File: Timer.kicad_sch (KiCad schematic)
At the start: 17 parts

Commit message: WIP solving ERC issues
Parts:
- added 10k211, 10k212, 10k213, 10k214, 10k215: R, symbol z80-rescue:R
- P202: renamed from P?; symbol z80-rescue:CONN_01X04 -> Connector:Conn_01x04_Pin
- gave numbers to parts that had none: 7
- renumbered 10k to 10k201, 10k to 10k202, 10k to 10k203, 10k to 10k204, 10k to 10k205, 10k to 10k206, 10k to 10k207, 10k to 10k208, 10k to 10k210
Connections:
- net A0: now also U202.34 (B/~{A})
- net A1: now also U202.33 (C/~{D})
- net CLK: now also U202.20 (CLK)
- net GND: now also U201.5 (GND), U202.31 (GND), 10k211.1
- net VCC: now also U201.24 (VCC), U202.9 (VCC), 10k212.1, 10k213.1, 10k214.1, 10k215.1
- net ~{RESET}: now also U202.21 (~{RESET})
- net D4: now reaches U201.1 (D4)
- net D4: now also U202.38 (D4)
- net ~{IORQ}: now reaches U201.10 (~{IORQ})
- net ~{IORQ}: now also U202.36 (~{IORQ})
- net IEO_CTC: now reaches P202.3 (Pin_3), U201.11 (IEO)
- net ~{INT_CTC}: now reaches P202.2 (Pin_2), U201.12 (~{INT})
- net IEI_CTC: now reaches P202.4 (Pin_4), U201.13 (IEI)
- net ~{M1}: now reaches U201.14 (~{M1})
- net ~{M1}: now also U202.8 (~{M1})
- net D5: now reaches U201.2 (D5)
- net D5: now also U202.3 (D5)
- net D0: now reaches U201.25 (D0)
- net D0: now also U202.40 (D0)
- net D1: now reaches U201.26 (D1)
- net D1: now also U202.1 (D1)
- net D2: now reaches U201.27 (D2)
- net D2: now also U202.39 (D2)
- net D3: now reaches U201.28 (D3)
- net D3: now also U202.2 (D3)
- net D6: now reaches U201.3 (D6)
- net D6: now also U202.37 (D6)
- net D7: now reaches U201.4 (D7)
- net D7: now also U202.4 (D7)
- net ~{RD}: now reaches U201.6 (~{RD})
- net ~{RD}: now also U202.32 (~{RD})
- net ZC/TO0: now reaches P204.1 (P1), U201.7 (ZC/TO0)
- net ZC/TO1: now reaches P204.2 (P2), U201.8 (ZC/TO1)
- net ZC/TO2: now reaches P204.3 (P3), U201.9 (ZC/TO2)
- net TxDA: now reaches P203.11 (P11)
- net TxDA: now also U202.15 (TxDA); no longer U202.10 (~{W}/~{RDYA})
- net ~{SYNCA}: now reaches 10k203.2, U202.11 (~{SYNCA})
- net ~{SYNCA}: now also P203.3 (P3); no longer P203.9 (P9)
- net RxDA: now reaches 10k209.2, U202.12 (RxDA)
- net RxDA: now also P203.5 (P5); no longer P203.1 (P1)
- net ~{RxCA}: now reaches 10k201.2, U202.13 (~{RxCA})
- net ~{RxCA}: now also P203.7 (P7); no longer P203.3 (P3)
- net ~{TxCA}: now reaches 10k202.2, U202.14 (~{TxCA})
- net ~{TxCA}: now also P203.9 (P9); no longer P203.7 (P7)
- net ~{CTSA}: now reaches P203.17 (P17)
- net ~{CTSA}: now also 10k204.2, U202.18 (~{CTSA}); no longer U202.16 (~{DTRA})
- net ~{DTRA}: now reaches P203.13 (P13)
- net ~{DTRA}: now also U202.16 (~{DTRA}); no longer U202.17 (~{RTSA})
- net ~{DCDA}: now reaches 10k206.2, P203.19 (P19), U202.19 (~{DCDA})
- net ~{DCDB}: now reaches U202.22 (~{DCDB})
- net ~{DCDB}: now also P203.18 (P18), 10k215.2
- net ~{CTSB}: now reaches U202.23 (~{CTSB})
- net ~{CTSB}: now also P203.16 (P16), 10k214.2
- net ~{RTSB}: now reaches U202.24 (~{RTSB})
- net ~{RTSB}: now also P203.14 (P14)
- net ~{DTRB}: now reaches U202.25 (~{DTRB})
- net ~{DTRB}: now also P203.12 (P12)
- net TxDB: now reaches U202.26 (TxDB)
- net TxDB: now also P203.10 (P10)
- net ~{RxTxCB}: now reaches U202.27 (~{RxTxCB})
- net ~{RxTxCB}: now also P203.8 (P8), 10k212.2
- net RxDB: now reaches U202.28 (RxDB)
- net RxDB: now also P203.6 (P6), 10k211.2
- net ~{SYNCB}: now reaches U202.29 (~{SYNCB})
- net ~{SYNCB}: now also P203.4 (P4), 10k213.2
- net ~{W}/~{RDYB}: now reaches U202.30 (~{W}/~{RDYB})
- net ~{W}/~{RDYB}: now also P203.2 (P2)
- net ~{SIO_CE}: now reaches U202.35 (~{CE})
- net ~{CE1} renamed ~{CTC_CE}
- new net ~{RTSA}: P203.15 (P15), U202.17 (~{RTSA})
- new net ~{W}/~{RDYA}: P203.1 (P1), U202.10 (~{W}/~{RDYA})
- no-connect marks 0 -> 1
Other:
- moved on the sheet: 10k201, 10k202, 10k203, 10k204, 10k206, 10k209, P203

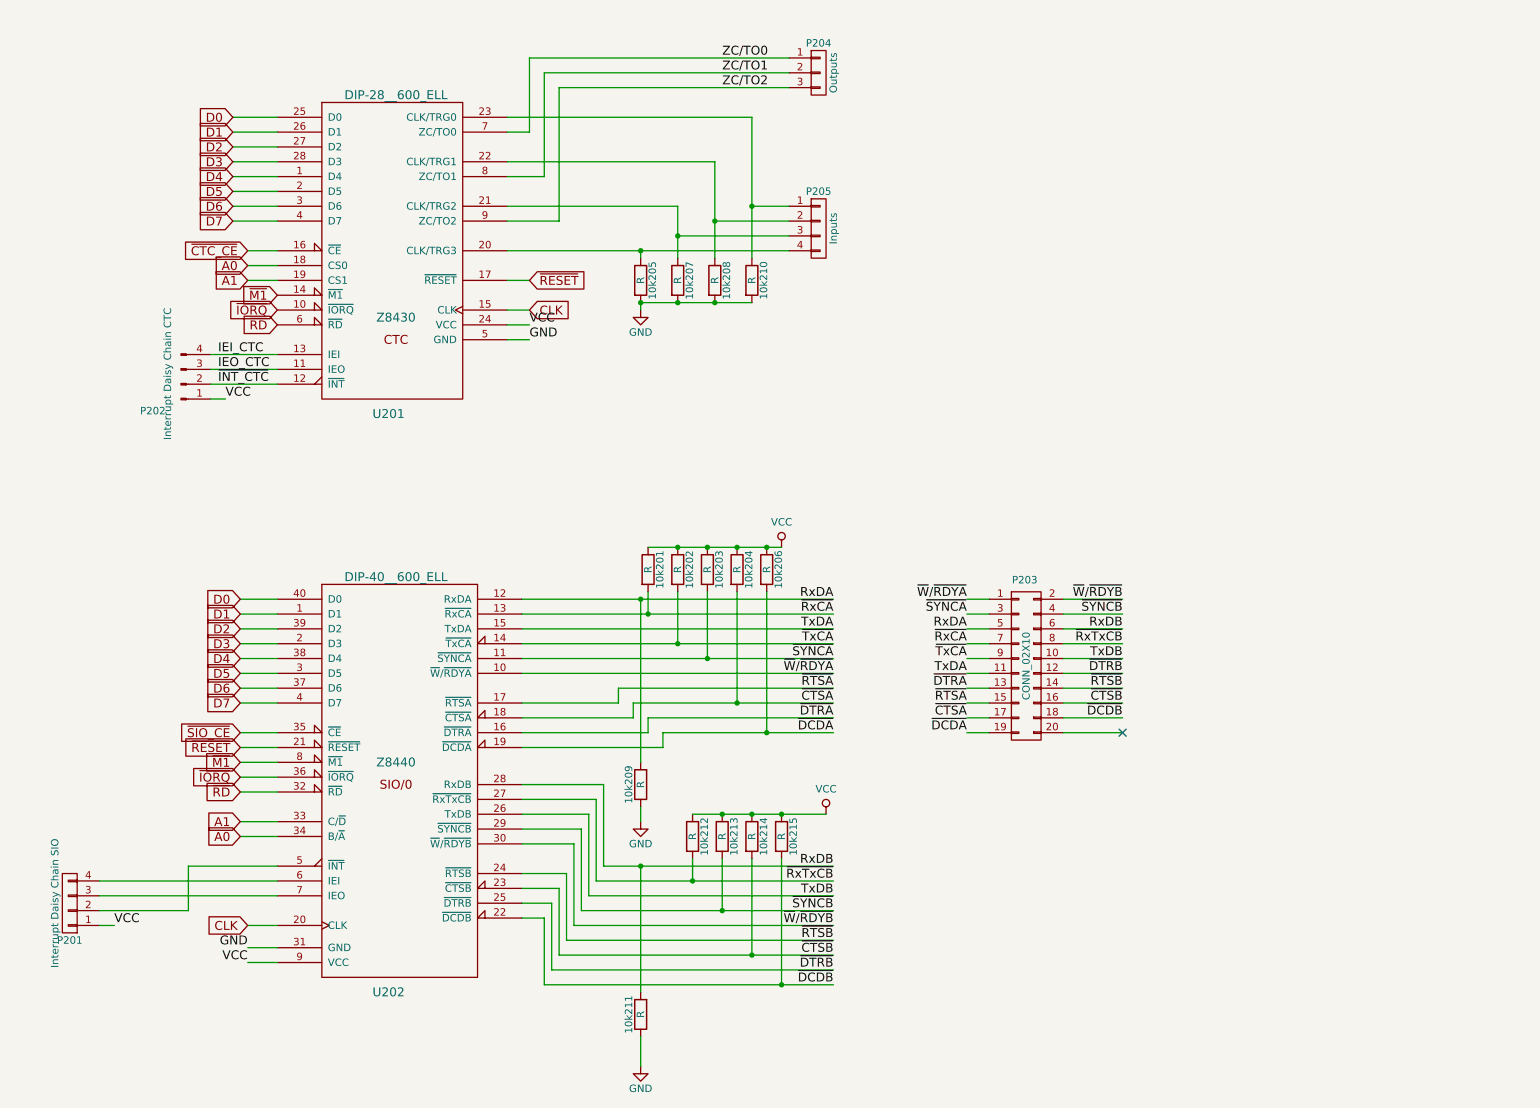
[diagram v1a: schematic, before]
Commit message: Fixed all schematic ERC errors and warnings
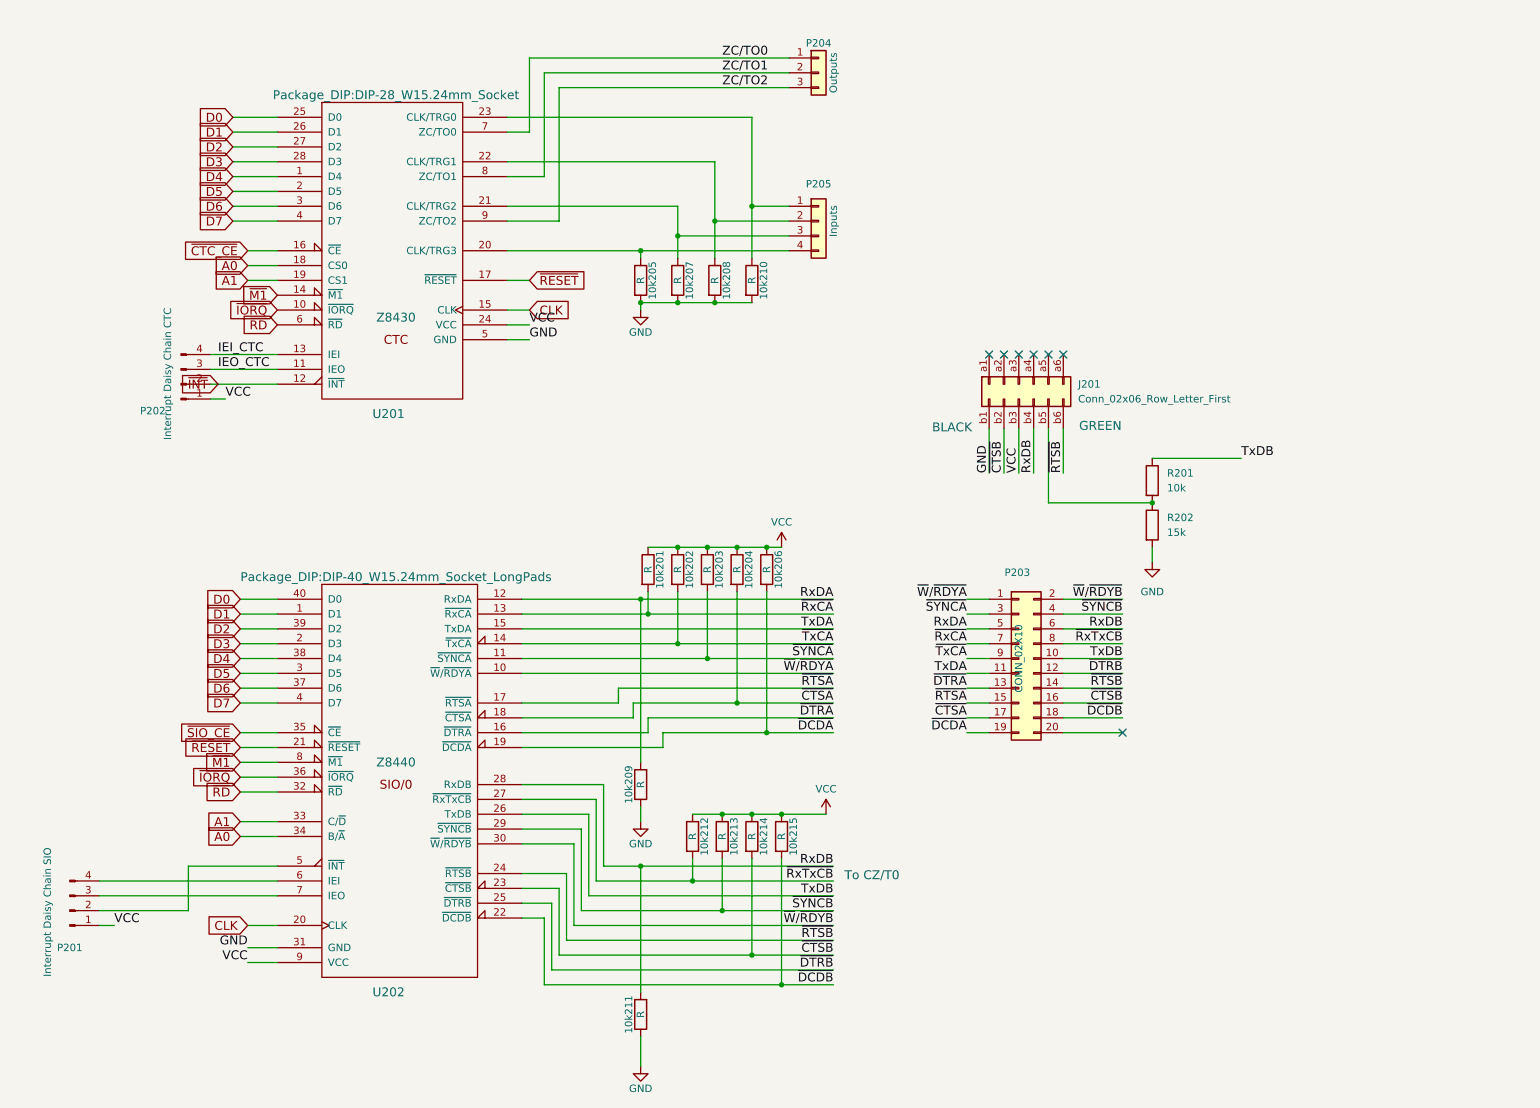
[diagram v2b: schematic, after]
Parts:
- added J201: Conn_02x06_Row_Letter_First, symbol Connector_Generic:Conn_02x06_Row_Letter_First
- added R201: 10k, symbol Device:R
- added R202: 15k, symbol Device:R
- 10k201, 10k202, 10k203, 10k204, 10k205, 10k206, 10k207, 10k208, 10k209, 10k210, 10k211, 10k212, 10k213, 10k214, 10k215: symbol z80-rescue:R -> Device:R
- P201: symbol z80-rescue:CONN_01X04 -> Connector:Conn_01x04_Pin
- P203: symbol z80-rescue:CONN_02X10 -> Connector_Generic:Conn_02x10_Odd_Even
- P204: symbol z80-rescue:CONN_01X03 -> Connector_Generic:Conn_01x03
- P205: symbol z80-rescue:CONN_01X04 -> Connector_Generic:Conn_01x04
- U201: footprint DIP-28__600_ELL -> Package_DIP:DIP-28_W15.24mm_Socket; symbol z80-rescue:Z8430 -> z80-ownSymbols:Z8430
- U202: footprint DIP-40__600_ELL -> Package_DIP:DIP-40_W15.24mm_Socket_LongPads; symbol z80-rescue:Z8440 -> z80-ownSymbols:Z8440
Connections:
- net GND: now also J201.b1 (Pin_b1), R202.2
- net RxDB: now also J201.b4 (Pin_b4)
- net TxDB: now also R201.1
- net VCC: now also J201.b3 (Pin_b3)
- net ~{CTSB}: now also J201.b2 (Pin_b2)
- net ~{RTSB}: now also J201.b6 (Pin_b6)
- net ~{INT_CTC} renamed ~{INT}
- new net: J201.b5 (Pin_b5), R201.2, R202.1
- no-connect marks 1 -> 7
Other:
- note added: "BLACK"
- note added: "GREEN"
- note added: "To CZ/T0"

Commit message: Started on pcb. WIP
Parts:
- added C201: 10u, Capacitor_THT:CP_Radial_D10.0mm_P5.00mm, symbol Device:C_Polarized
- 10k201, 10k202, 10k203, 10k204, 10k205, 10k206, 10k207, 10k208, 10k209, 10k210, 10k211, 10k212, 10k213, 10k214, 10k215, R201, R202: footprint (none) -> Resistor_SMD:R_0805_2012Metric_Pad1.20x1.40mm_HandSolder
- J201: footprint (none) -> Connector_PinHeader_2.54mm:PinHeader_2x06_P2.54mm_Vertical
- P201, P202, P205: footprint (none) -> Connector_PinHeader_2.54mm:PinHeader_1x04_P2.54mm_Vertical
- P203: footprint (none) -> Connector_PinHeader_2.54mm:PinHeader_2x10_P2.54mm_Vertical
- P204: footprint (none) -> Connector_PinHeader_2.54mm:PinHeader_1x03_P2.54mm_Vertical
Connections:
- net GND: now also C201.2
- net VCC: now also C201.1
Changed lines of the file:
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@@
 	(wire
 		(pts
+			(xy 247.65 43.18) (xy 254 43.18)
+		)
+		(stroke
+			(width 0)
+			(type default)
+		)
+	)
+	(wire
+		(pts
 			(xy 124.46 170.18) (xy 130.81 170.18)
 		)
@@
 	(wire
 		(pts
+			(xy 247.65 35.56) (xy 254 35.56)
+		)
+		(stroke
+			(width 0)
+			(type default)
+		)
+	)
+	(wire
+		(pts
 			(xy 152.4 115.57) (xy 154.94 115.57)
 		)
@@
 		)
 	)
+	(label "VCC"
+		(at 247.65 35.56 0)
+		(effects
+			(font
+				(size 1.524 1.524)
+			)
+			(justify left bottom)
+		)
+	)
 	(label "~{DTRA}"
 		(at 163.83 144.78 180)
@@
 		)
 	)
+	(label "GND"
+		(at 247.65 43.18 0)
+		(effects
+			(font
+				(size 1.524 1.524)
+			)
+			(justify left bottom)
+		)
+	)
 	(label "~{SYNCB}"
 		(at 163.83 177.8 180)
@@
 			)
 		)
-		(property "Footprint" ""
+		(property "Footprint" "Connector_PinHeader_2.54mm:PinHeader_1x04_P2.54mm_Vertical"
 			(at 52.07 87.63 0)
 			(effects
@@
 			)
 		)
-		(property "Footprint" ""
+		(property "Footprint" "Connector_PinHeader_2.54mm:PinHeader_1x03_P2.54mm_Vertical"
 			(at 161.29 34.29 0)
 			(effects
@@
 			)
 		)
-		(property "Footprint" ""
+		(property "Footprint" "Connector_PinHeader_2.54mm:PinHeader_1x04_P2.54mm_Vertical"
 			(at 161.29 59.69 0)
 			(effects
@@
 			)
 		)
-		(property "Footprint" ""
+		(property "Footprint" "Resistor_SMD:R_0805_2012Metric_Pad1.20x1.40mm_HandSolder"
 			(at 129.032 69.85 90)
 			(effects
@@
 			)
 		)
-		(property "Footprint" ""
+		(property "Footprint" "Resistor_SMD:R_0805_2012Metric_Pad1.20x1.40mm_HandSolder"
 			(at 135.382 69.85 90)
 			(effects
@@
 			)
 		)
-		(property "Footprint" ""
+		(property "Footprint" "Resistor_SMD:R_0805_2012Metric_Pad1.20x1.40mm_HandSolder"
 			(at 141.732 69.85 90)
 			(effects
@@
 			)
 		)
-		(property "Footprint" ""
+		(property "Footprint" "Resistor_SMD:R_0805_2012Metric_Pad1.20x1.40mm_HandSolder"
 			(at 148.082 69.85 90)
 			(effects
@@
 			)
 		)
-		(property "Footprint" ""
+		(property "Footprint" "Connector_PinHeader_2.54mm:PinHeader_1x04_P2.54mm_Vertical"
 			(at 33.02 177.8 0)
 			(effects
@@
 			)
 		)
-		(property "Footprint" ""
+		(property "Footprint" "Connector_PinHeader_2.54mm:PinHeader_2x10_P2.54mm_Vertical"
 			(at 195.58 134.62 0)
 			(effects
@@
 			)
 		)
-		(property "Footprint" ""
+		(property "Footprint" "Resistor_SMD:R_0805_2012Metric_Pad1.20x1.40mm_HandSolder"
 			(at 130.302 119.38 90)
 			(effects
@@
 			)
 		)
-		(property "Footprint" ""
+		(property "Footprint" "Resistor_SMD:R_0805_2012Metric_Pad1.20x1.40mm_HandSolder"
 			(at 135.382 119.38 90)
 			(effects
@@
 			)
 		)
-		(property "Footprint" ""
+		(property "Footprint" "Resistor_SMD:R_0805_2012Metric_Pad1.20x1.40mm_HandSolder"
 			(at 140.462 119.38 90)
 			(effects
@@
 			)
 		)
-		(property "Footprint" ""
+		(property "Footprint" "Resistor_SMD:R_0805_2012Metric_Pad1.20x1.40mm_HandSolder"
 			(at 145.542 119.38 90)
 			(effects
@@
 			)
 		)
-		(property "Footprint" ""
+		(property "Footprint" "Resistor_SMD:R_0805_2012Metric_Pad1.20x1.40mm_HandSolder"
 			(at 150.622 119.38 90)
 			(effects
@@
 			)
 		)
-		(property "Footprint" ""
+		(property "Footprint" "Resistor_SMD:R_0805_2012Metric_Pad1.20x1.40mm_HandSolder"
 			(at 132.588 156.21 90)
 			(effects
@@
 			)
 		)
-		(property "Footprint" ""
+		(property "Footprint" "Resistor_SMD:R_0805_2012Metric_Pad1.20x1.40mm_HandSolder"
 			(at 216.662 111.76 90)
 			(effects
@@
 	)
 	(symbol
+		(lib_id "Device:C_Polarized")
+		(at 254 39.37 0)
+		(unit 1)
+		(exclude_from_sim no)
+		(in_bom yes)
+		(on_board yes)
+		(dnp no)
+		(fields_autoplaced yes)
+		(property "Reference" "C201"
+			(at 257.81 37.2109 0)
+			(effects
+				(font
+					(size 1.27 1.27)
+				)
+				(justify left)
+			)
+		)
+		(property "Value" "10u"
+			(at 257.81 39.7509 0)
+			(effects
+				(font
+					(size 1.27 1.27)
+				)
+				(justify left)
+			)
+		)
+		(property "Footprint" "Capacitor_THT:CP_Radial_D10.0mm_P5.00mm"
+			(at 254.9652 43.18 0)
+			(effects
+				(font
+					(size 1.27 1.27)
+				)
+				(hide yes)
+			)
+		)
+		(property "Datasheet" "~"
+			(at 254 39.37 0)
+			(effects
+				(font
+					(size 1.27 1.27)
+				)
+				(hide yes)
+			)
+		)
+		(property "Description" "Polarized capacitor"
+			(at 254 39.37 0)
+			(effects
+				(font
+					(size 1.27 1.27)
+				)
+				(hide yes)
+			)
+		)
+		(pin "1"
+		)
+		(pin "2"
+		)
+		(instances
+			(project "z80"
+				(path "/e7eeb274-d662-49f9-a7ce-d4911c9f2b64/00000000-0000-0000-0000-0000568ed54e"
+					(reference "C201")
+					(unit 1)
+				)
+			)
+		)
+	)
+	(symbol
 		(lib_id "Device:R")
 		(at 154.94 165.1 0)
@@
 			)
 		)
-		(property "Footprint" ""
+		(property "Footprint" "Resistor_SMD:R_0805_2012Metric_Pad1.20x1.40mm_HandSolder"
 			(at 153.162 165.1 90)
 			(effects
@@
 			)
 		)
-		(property "Footprint" ""
+		(property "Footprint" "Resistor_SMD:R_0805_2012Metric_Pad1.20x1.40mm_HandSolder"
 			(at 137.922 165.1 90)
 			(effects
@@
 			)
 		)
-		(property "Footprint" ""
+		(property "Footprint" "Resistor_SMD:R_0805_2012Metric_Pad1.20x1.40mm_HandSolder"
 			(at 216.662 104.14 90)
 			(effects
@@
 			)
 		)
-		(property "Footprint" ""
+		(property "Footprint" "Resistor_SMD:R_0805_2012Metric_Pad1.20x1.40mm_HandSolder"
 			(at 148.082 165.1 90)
 			(effects
@@
 			)
 		)
-		(property "Footprint" ""
+		(property "Footprint" "Resistor_SMD:R_0805_2012Metric_Pad1.20x1.40mm_HandSolder"
 			(at 143.002 165.1 90)
 			(effects
@@
 			)
 		)
-		(property "Footprint" ""
+		(property "Footprint" "Connector_PinHeader_2.54mm:PinHeader_2x06_P2.54mm_Vertical"
 			(at 195.58 87.63 0)
 			(effects
@@
 			)
 		)
-		(property "Footprint" ""
+		(property "Footprint" "Resistor_SMD:R_0805_2012Metric_Pad1.20x1.40mm_HandSolder"
 			(at 132.588 195.58 90)
 			(effects
